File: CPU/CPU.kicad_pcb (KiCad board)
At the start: 2 copper layers, 157.1 x 85.3 mm, 112 parts, among them J101 Conn_02x10_Odd_Even, J102 Conn_01x07_Female, J201 Conn_02x03_Odd_Even, J302 1X4SMD-FPC, J303 Conn_02x03_Odd_Even, Q101 IRLML0040TR, Q102 IRLML0040TR, Q201 DMC4050, Q202 IRLML0040TR, Q301 IRLML0040TR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

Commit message: V5 Sent to fab.
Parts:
- SW101: footprint Marco:SWITCH_PCM12SMTR_SPDT -> MarcoK:SWITCH_SS312SAH4_SPDT
- moved C211 3.58 mm to (142.5, 123.5), turned to 0 degrees
- moved SW101 1.25 mm to (148.2, 126.8)
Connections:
- SW101 pad 1: +5VP -> 5V
- SW101 pad 3: 5V -> +5VP
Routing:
- net /Pi5V: track 41.1 -> 37.6 mm
- net +5VP: track 8.33 -> 11.2 mm
- net /Micro Controller Devices/SWW: track 65.7 -> 63.9 mm
- net 5V: track 543.9 -> 542.3 mm
- net GND: vias 321 -> 318
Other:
- board text added: "CR101 CPU Board V5 mquezada 20200806"
- board text added: "D/C"
- board text added: "LCD_PW"
- board text added: "PiRX"
- board text added: "PiTX"
- board text added: "RT_CS"
- board text added: "TAPE FOR PI"
- board text removed: "CR101 CPU Board V4 mquezada 20200717"
- board text removed: "DC"

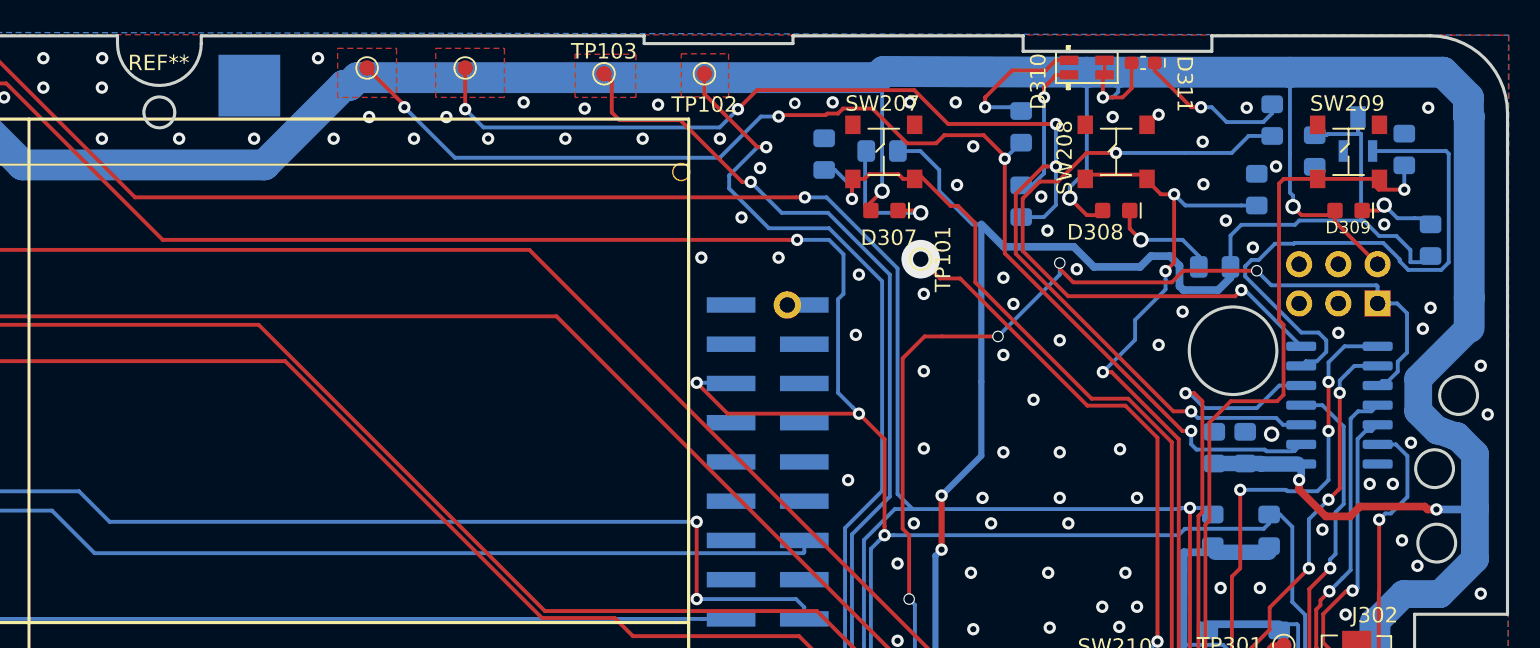
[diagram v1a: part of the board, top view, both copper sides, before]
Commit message: Moved LED up a bit. Increased buffer space around mounting hole to keep vias away from screw head. It's alive! With RPi and LCD on board. Still need to get scroll wheel to connect.
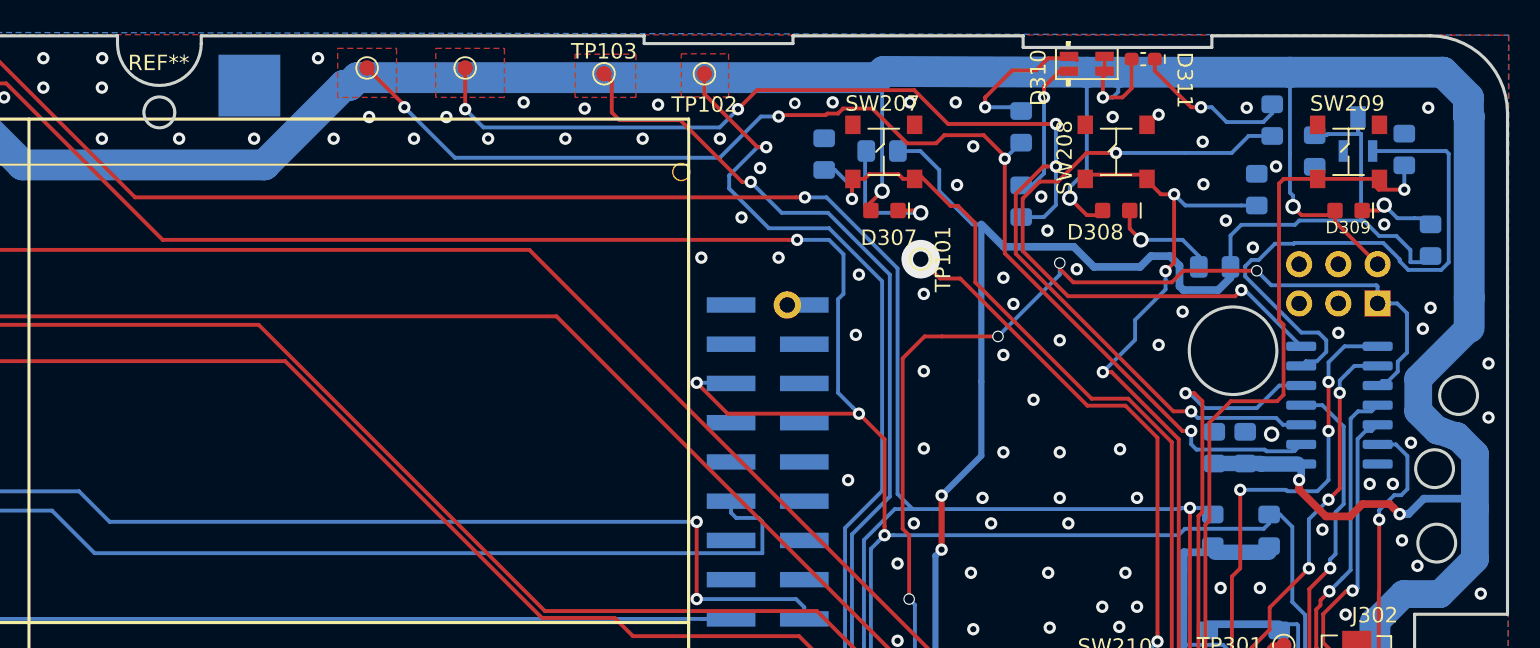
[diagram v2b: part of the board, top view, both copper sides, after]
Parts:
- moved D310 0.25 mm to (160.2, 47.4)
- moved D311 0.25 mm to (163.9, 47.0)
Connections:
- Pi101 pad 28: /TFT_DC -> Net-(Pi101-Pad28)
- Pi101 pad 29: /LCD_PWR -> /TFT_DC
- Pi101 pad 31: Net-(Pi101-Pad31) -> /LCD_PWR
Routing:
- net /TFT_DC: track 68.6 -> 70.2 mm
- net 5V: track 542.3 -> 543.4 mm
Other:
- outline, holes or cut-outs redrawn
